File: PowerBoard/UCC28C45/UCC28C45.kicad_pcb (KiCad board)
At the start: 2 copper layers, 45 x 75 mm, 34 parts, among them J1 AuxConn, Q1 GT10N10, U2 UCC28C45D

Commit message: ucc fixes
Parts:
- R10: value 4k -> 3.9k
- R11: value 8.2 -> 10; footprint Resistor_SMD:R_0805_2012Metric -> Resistor_SMD:R_0603_1608Metric
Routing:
- net Net-(C12-Pad2): track 0.00 -> 1.80 mm
- net Net-(C11-Pad2): track 0.00 -> 1.80 mm
- net GNDD: track 0.53 -> 1.00 mm, vias 11 -> 18
- net -BATT: vias 92 -> 94

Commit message: ucc fixes
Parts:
- removed D3: SS115, Diode_SMD:D_SMA
- added D1: RUN, Diode_SMD:D_0603_1608Metric, B.Cu at (91.8, 122.5)
- added J2: POWER_SW, Connector_JST:JST_XH_B4B-XH-A_1x04_P2.50mm_Vertical, F.Cu at (92.0, 95.0)
- added JP1: CompCut, Jumper:SolderJumper-2_P1.3mm_Bridged_Pad1.0x1.5mm, B.Cu at (77.8, 127.2)
- added Q2: AO3400A, Package_TO_SOT_SMD:SOT-23, B.Cu at (75.2, 122.2)
- added R13: 1k, Resistor_SMD:R_1206_3216Metric, B.Cu at (88.8, 118.5)
- added R14: 10k, Resistor_SMD:R_0603_1608Metric, B.Cu at (78.0, 122.5)
- added R15: 82k, Resistor_SMD:R_0603_1608Metric, B.Cu at (91.8, 125.5)
- added R16: 10k, Resistor_SMD:R_0603_1608Metric, B.Cu at (90.2, 121.2)
- added R5: 100, Resistor_SMD:R_0603_1608Metric, B.Cu at (76.8, 124.8)
- D2, D4: value SS115 -> SS320BF; footprint Diode_SMD:D_SMA -> Diode_SMD:D_SMB
- Q1: value GT10N10 -> BSC520N15NS3G; footprint Package_TO_SOT_SMD:TO-252-2 -> Package_TO_SOT_SMD:TDSON-8-1
- U2: value UCC28C45D -> UC3845BD1013TR
- moved C15 16.5 mm to (81.8, 130.5)
- moved D4 5.22 mm to (81.2, 124.8)
- moved R1 5.06 mm to (90.8, 107.0), turned to -90 degrees
- moved R3 4.92 mm to (67.5, 129.2), turned to 180 degrees
- moved R11 4.74 mm to (67.8, 125.5)
- moved R12 4.67 mm to (68.5, 123.2), turned to 180 degrees
- moved R10 3.82 mm to (73.0, 125.0)
- moved Q1 3.60 mm to (69.5, 118.0)
- moved R7 2.25 mm to (77.2, 132.8), turned to -90 degrees
- moved C11 1.90 mm to (78.2, 114.2)
- moved C12 1.90 mm to (78.2, 111.8)
- moved C3 1.90 mm to (83.0, 111.8)
- moved C4 1.90 mm to (83.0, 114.2)
- moved D2 1.75 mm to (60.8, 130.8)
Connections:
- C16 pad 2: Net-(U2-COMP) -> Net-(JP1-B)
- Q1 pad 1: Net-(Q1-G) -> GNDD
- Q1 pad 2: +BATT -> GNDD
- R3 pad 1: +BATT -> VDD
- R3 pad 2: VDD -> +BATT
- R8 pad 1: Net-(U2-COMP) -> Net-(JP1-B)
- U2 pad 1: Net-(U2-COMP) -> Net-(JP1-A)
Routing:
- net Net-(J2-Pin_4): track 0.00 -> 43.8 mm, vias 0 -> 2
- net GNDD: track 1.00 -> 43.6 mm, vias 18 -> 25
- net Net-(J2-Pin_2): track 0.00 -> 36.4 mm
- net VDD: track 28.7 -> 42.6 mm, vias 0 -> 2
- net Net-(JP1-A): track 0.00 -> 12.6 mm
- net OUT: track 5.53 -> 10.8 mm
- net Net-(Q2-G): track 0.00 -> 5.15 mm
- net IN_V: track 7.38 -> 3.38 mm
- net Net-(U2-VREF): track 15.3 -> 11.5 mm
- net Net-(JP1-B): track 0.00 -> 3.72 mm
- net Net-(U2-COMP): track 3.24 -> 0.00 mm
- net FB: track 14.3 -> 12.2 mm
- net Net-(D1-K): track 0.00 -> 1.39 mm
- net Net-(Q1-G): track 4.89 -> 3.80 mm
- net +12V: track 24.4 -> 25.0 mm, vias 2 -> 5
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
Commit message: v2.10.0 - Release
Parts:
- removed C8: 330u 150V, Capacitor_THT:CP_Radial_D16.0mm_P7.50mm
- moved C10 4.51 mm to (67.0, 104.5)
- moved C2 4.51 mm to (67.0, 87.5)
- moved C7 0.56 mm to (76.0, 104.2)
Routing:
- net -BATT: vias 120 -> 104
- net +BATT: vias 28 -> 27
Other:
- board size 45 x 75 mm -> 40 x 75 mm
- board text added: "GigaESC - UC3845 Designed by Kaminaris v1.0.0 - 200V -> 12V"

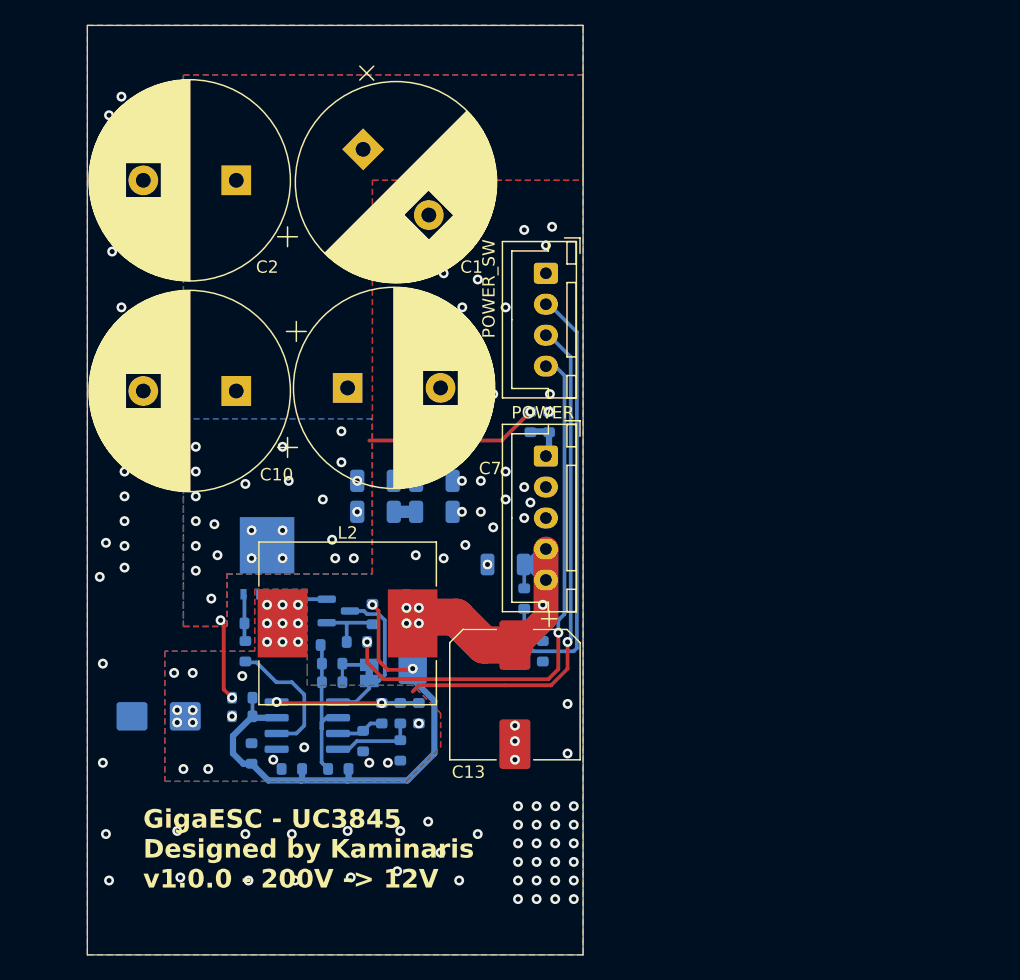
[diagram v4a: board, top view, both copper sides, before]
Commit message: v3.0.1 - GaN redesign
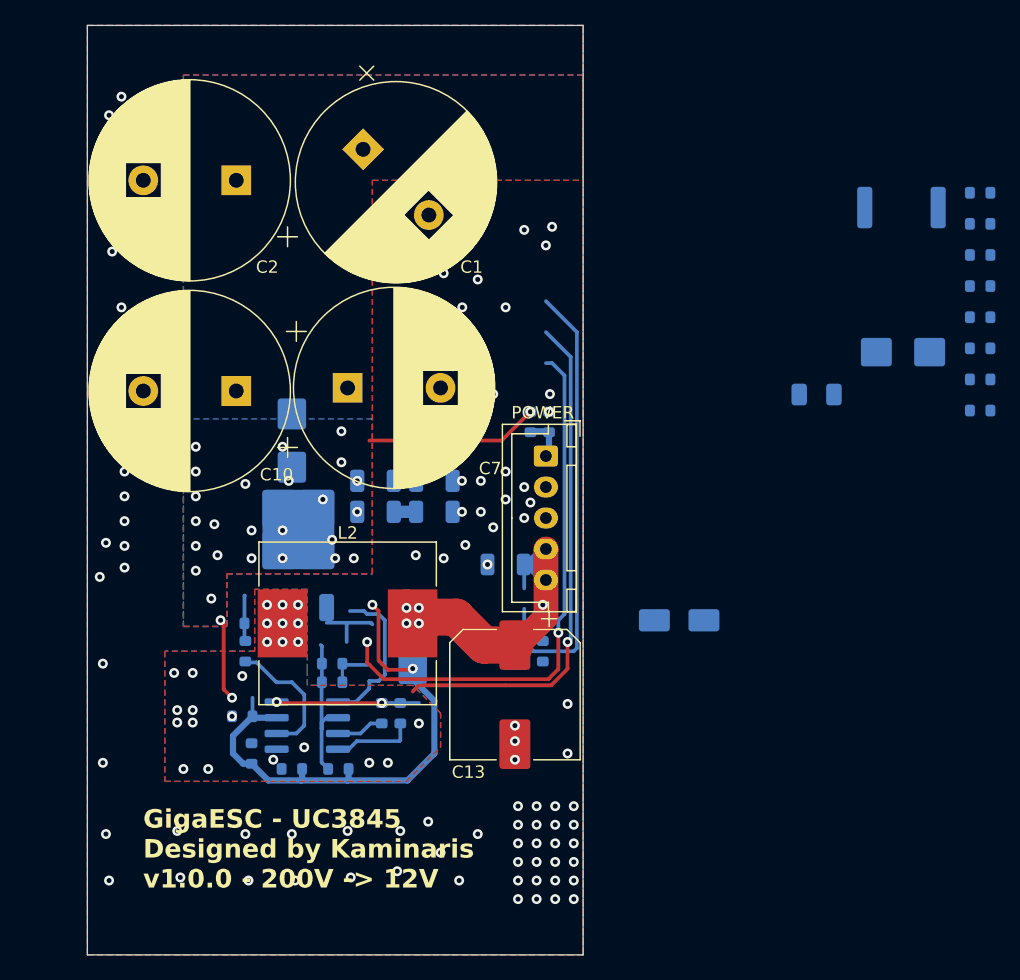
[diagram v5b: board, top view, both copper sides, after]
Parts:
- removed C14: 470p, GigaVescLibs:C_0603_1608Metric_L
- removed C15: 1u, GigaVescLibs:C_0603_1608Metric_L
- removed J2: POWER_SW, Connector_JST:JST_XH_B4B-XH-A_1x04_P2.50mm_Vertical
- removed JP1: CompCut, Jumper:SolderJumper-2_P1.3mm_Bridged_Pad1.0x1.5mm
- removed Q1: BSC520N15NS3G, Package_TO_SOT_SMD:TDSON-8-1
- removed R10: 3.9k, Resistor_SMD:R_0603_1608Metric
- removed R14, R16: 10k, Resistor_SMD:R_0603_1608Metric
- removed R3: 5.1k, Resistor_SMD:R_0603_1608Metric
- removed R5: 100, Resistor_SMD:R_0603_1608Metric
- removed R7: 1k, Resistor_SMD:R_0603_1608Metric
- removed U2: UC3845BD1013TR, Package_SO:SOIC-8_3.9x4.9mm_P1.27mm
- added C18: 10n, GigaVescLibs:C_0603_1608Metric_L, B.Cu at (127.0, 93.5)
- added C19: 100n, GigaVescLibs:C_0603_1608Metric_L, B.Cu at (127.0, 96.0)
- added C20: 2.2u, GigaVescLibs:C_0603_1608Metric_L, B.Cu at (127.0, 98.5)
- added C6: 2.2n, GigaVescLibs:C_0603_1608Metric_L, B.Cu at (127.0, 88.5)
- added C8: 100n, GigaVescLibs:C_0603_1608Metric_L, B.Cu at (127.0, 91.0)
- added D3: SS520BF, Diode_SMD:D_SMB, B.Cu at (120.8, 101.4)
- added D5: 15V, Diode_SMD:D_SMA, B.Cu at (102.8, 123.0)
- added F1: 3A, Fuse:Fuse_1206_3216Metric, B.Cu at (113.8, 104.8)
- added R17: 10k, Resistor_SMD:R_0603_1608Metric, B.Cu at (127.0, 101.1)
- added R18: 5.1k, Resistor_SMD:R_0603_1608Metric, B.Cu at (127.0, 103.6)
- added R19: 27k, Resistor_SMD:R_0603_1608Metric, B.Cu at (127.0, 106.1)
- added R20: 50m, Resistor_SMD:R_2512_6332Metric, B.Cu at (120.7, 89.7)
- added U1: UC3845BD1013TR, Package_SO:SOIC-8_3.9x4.9mm_P1.27mm, B.Cu at (72.8, 131.5)
- C16: value 470p -> 330p
- D2, D4: value SS320BF -> SS520BF
- Q2: value AO3400A -> IRFR13N20DTRPBF; footprint Package_TO_SOT_SMD:SOT-23 -> Package_TO_SOT_SMD:TO-252-2
- R11: value 10 -> 2.2
- R12: value 10k -> 390
- R15: value 82k -> 20k
- moved D2 24.7 mm to (71.5, 108.5), turned to 90 degrees
- moved Q2 6.22 mm to (72.0, 116.9), turned to 90 degrees
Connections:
- net VDD renamed Net-(D4-K)
- C13 pad 1: +12V -> Net-(D1-A)
- C16 pad 1: FB -> Net-(U1-COMP)
- C16 pad 2: Net-(JP1-B) -> Net-(U1-FB)
- D1 pad 2: +12V -> Net-(D1-A)
- D2 pad 1: GNDD -> Net-(D2-K)
- D2 pad 2: -BATT -> +BATT
- D4 pad 2: +12V -> Net-(D1-A)
- L2 pad 2: +12V -> Net-(D1-A)
- Q2 pad 2: GNDD -> Net-(D2-K)
- Q2 pad 3: Net-(JP1-A) -> Net-(Q2-S)
- R11 pad 1: OUT -> Net-(U1-OUT)
- R11 pad 2: Net-(Q1-G) -> Net-(Q2-G)
- R12 pad 1: GNDD -> Net-(D1-A)
- R12 pad 2: Net-(Q1-G) -> -BATT
- R13 pad 1: +12V -> Net-(U1-CS)
- R13 pad 2: -BATT -> Net-(Q2-S)
- R4 pad 1: CS -> VREF
- R4 pad 2: Net-(U2-VREF) -> Net-(U1-RC)
- R6 pad 1: Net-(U2-RT/CT) -> Net-(U1-FB)
- R6 pad 2: Net-(U2-VREF) -> GNDD
- R8 pad 1: Net-(JP1-B) -> Net-(U1-FB)
- R8 pad 2: FB -> Net-(U1-COMP)
- R9 pad 1: FB -> Net-(U1-FB)
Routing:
- net (no net): track 0.00 -> 155.5 mm, vias 0 -> 3
- net Net-(J2-Pin_4): track 43.8 -> 0.00 mm, vias 2 -> 0
- net GNDD: track 43.6 -> 0.00 mm, vias 25 -> 22
- net Net-(J2-Pin_2): track 36.4 -> 0.00 mm
- net Net-(U1-COMP): track 0.00 -> 12.6 mm
- net Net-(JP1-A): track 12.6 -> 0.00 mm
- net FB: track 12.2 -> 0.00 mm
- net Net-(U2-VREF): track 11.5 -> 0.00 mm, vias 2 -> 0
- net OUT: track 10.8 -> 0.00 mm
- net Net-(U1-OUT): track 0.00 -> 10.8 mm
- net Net-(U2-RT/CT): track 6.68 -> 0.00 mm
- net VREF: track 0.00 -> 3.86 mm
- net CS: track 3.86 -> 0.00 mm
- net Net-(Q1-G): track 3.80 -> 0.00 mm
- net Net-(U1-FB): track 0.00 -> 3.72 mm
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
